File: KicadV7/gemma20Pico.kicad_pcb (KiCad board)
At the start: 2 copper layers, 60 x 45 mm, 10 parts, among them J1-Prox1 I2C_CH0, J2-Prox0 I2C_CH1, J3-Motor1 DC-Motor, J4-BAT1 3.7V Battery, J5-Servo1 Servo, J6-Pot1 Pot, J7-Pot2 Pot, U1-RPI-Pico1 Pico

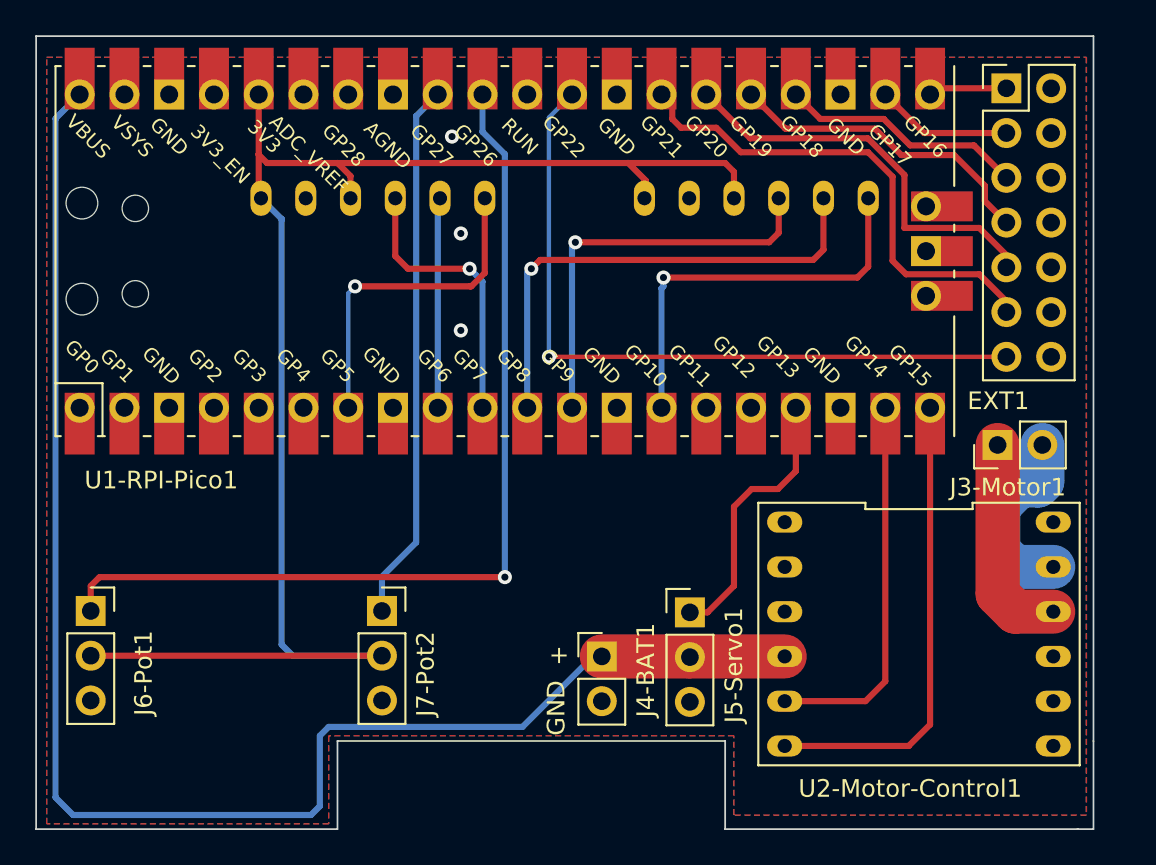
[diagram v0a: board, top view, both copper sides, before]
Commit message: Connect H bridges in paralell
Connect H-Bridges in paralell for 2xcurrent, added mounting holes , reduced board size to allow G9 Servo mount moved  and rotated  POT  for easyer access to +3.3V
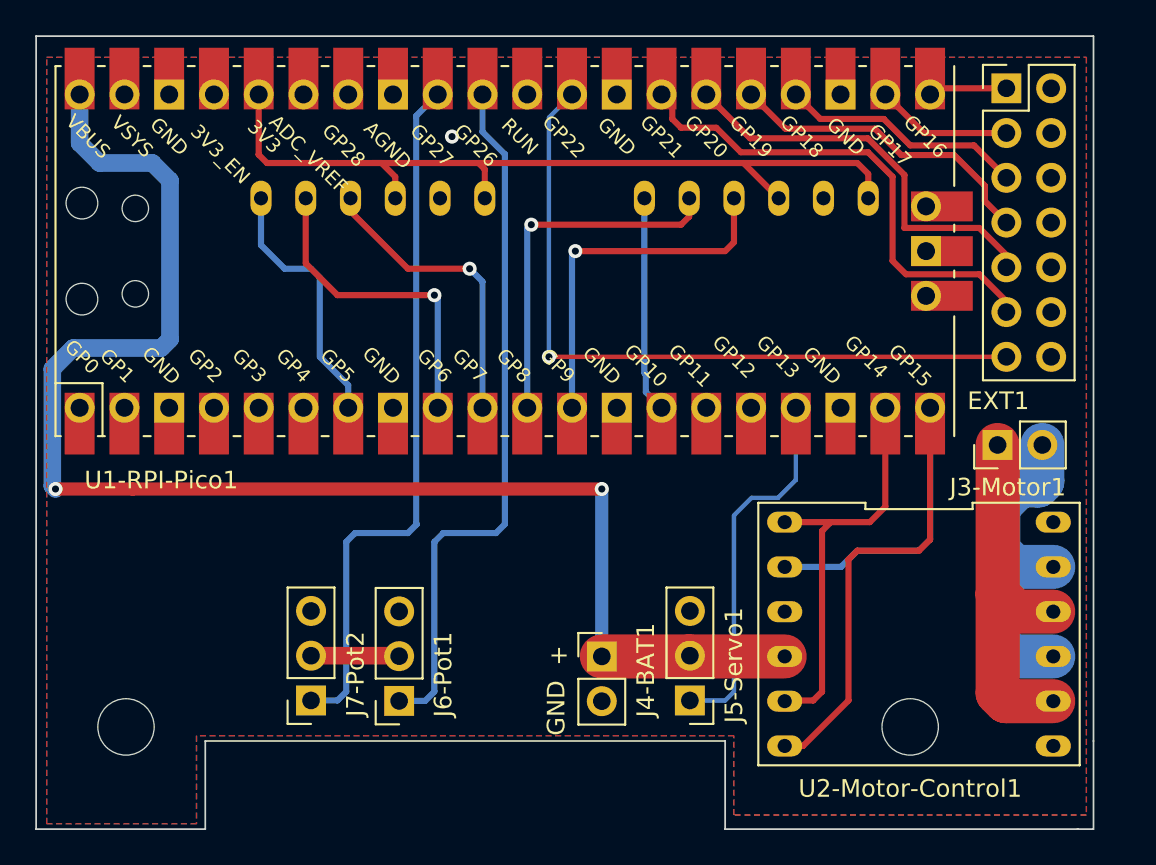
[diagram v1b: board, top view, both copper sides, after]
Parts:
- added REF**: M3_ISO14580, MountingHole:MountingHole_3.2mm_M3_ISO14580, F.Cu at (139.5, 119.5)
- added REF**: M3_ISO14580, MountingHole:MountingHole_3.2mm_M3_ISO14580, F.Cu at (95.0, 119.5)
- moved J6-Pot1 18.2 mm to (110.5, 118.0), turned to 180 degrees
- moved J7-Pot2 6.48 mm to (105.5, 118.0), turned to 180 degrees
- moved J5-Servo1 5.00 mm to (127.0, 118.0), turned to 180 degrees
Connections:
- J3-Motor1 pad 1: Net-(J3-Motor1-Pin_1) -> /MO2
- J3-Motor1 pad 2: Net-(J3-Motor1-Pin_2) -> /MO1
- U2-Motor-Control1 pad 1: unconnected-(U2-Motor-Control1-IN4-Pad1) -> /MC_2
- U2-Motor-Control1 pad 10: Net-(J3-Motor1-Pin_1) -> /MO2
- U2-Motor-Control1 pad 11: Net-(J3-Motor1-Pin_2) -> /MO1
- U2-Motor-Control1 pad 2: unconnected-(U2-Motor-Control1-IN3-Pad2) -> /MC_1
- U2-Motor-Control1 pad 8: unconnected-(U2-Motor-Control1-OUT4-Pad8) -> /MO2
- U2-Motor-Control1 pad 9: unconnected-(U2-Motor-Control1-OUT3-Pad9) -> /MO1
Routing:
- net +3.3V: track 87.9 -> 52.7 mm
- net /MO2: track 0.00 -> 21.0 mm
- net /MO1: track 0.00 -> 20.0 mm
- net /MC_1: track 26.7 -> 41.6 mm
- net /ADC0: track 53.0 -> 40.0 mm, vias 1 -> 0
- net Net-(J3-Motor1-Pin_1): track 12.0 -> 0.00 mm
- net Net-(J3-Motor1-Pin_2): track 11.2 -> 0.00 mm
- net /ADC1: track 30.6 -> 41.7 mm
- net /INT0: track 23.2 -> 12.3 mm, vias 1 -> 0
- net /SDA0: track 27.9 -> 20.7 mm
- net /SDA1: track 11.9 -> 18.2 mm, vias 0 -> 1
- net /Servo_SIGN: track 15.6 -> 21.1 mm
- net +BATT: track 88.4 -> 83.5 mm, vias 0 -> 2
- net /INT1: track 19.0 -> 15.0 mm, vias 1 -> 0
- net /SCL0: track 23.2 -> 20.7 mm
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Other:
- outline, holes or cut-outs redrawn
- board text added: "PicoRC 1.1 Jan & Rune"
- board text removed: "Jan & Rune"
- board text removed: "RC Car CTRL V1.0"
